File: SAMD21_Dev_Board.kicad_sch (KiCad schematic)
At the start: 76 parts, among them J1 SWD, J10 JST_SH_SM06B-SRSS-TB_1x06-1MP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, J11 JST_SH_SM06B-SRSS-TB_1x06-1MP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, J12 JST_SH_SM06B-SRSS-TB_1x06-1MP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, J13 JST_SH_SM06B-SRSS-TB_1x06-1MP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, J14 JST_SH_SM06B-SRSS-TB_1x06-1MP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, J15 JST_SH_SM06B-SRSS-TB_1x06-1MP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, J16 JST_SH_SM06B-SRSS-TB_1x06-1MP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, J17 Status LED, J2 USB_C_Receptacle_USB2.0_16P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

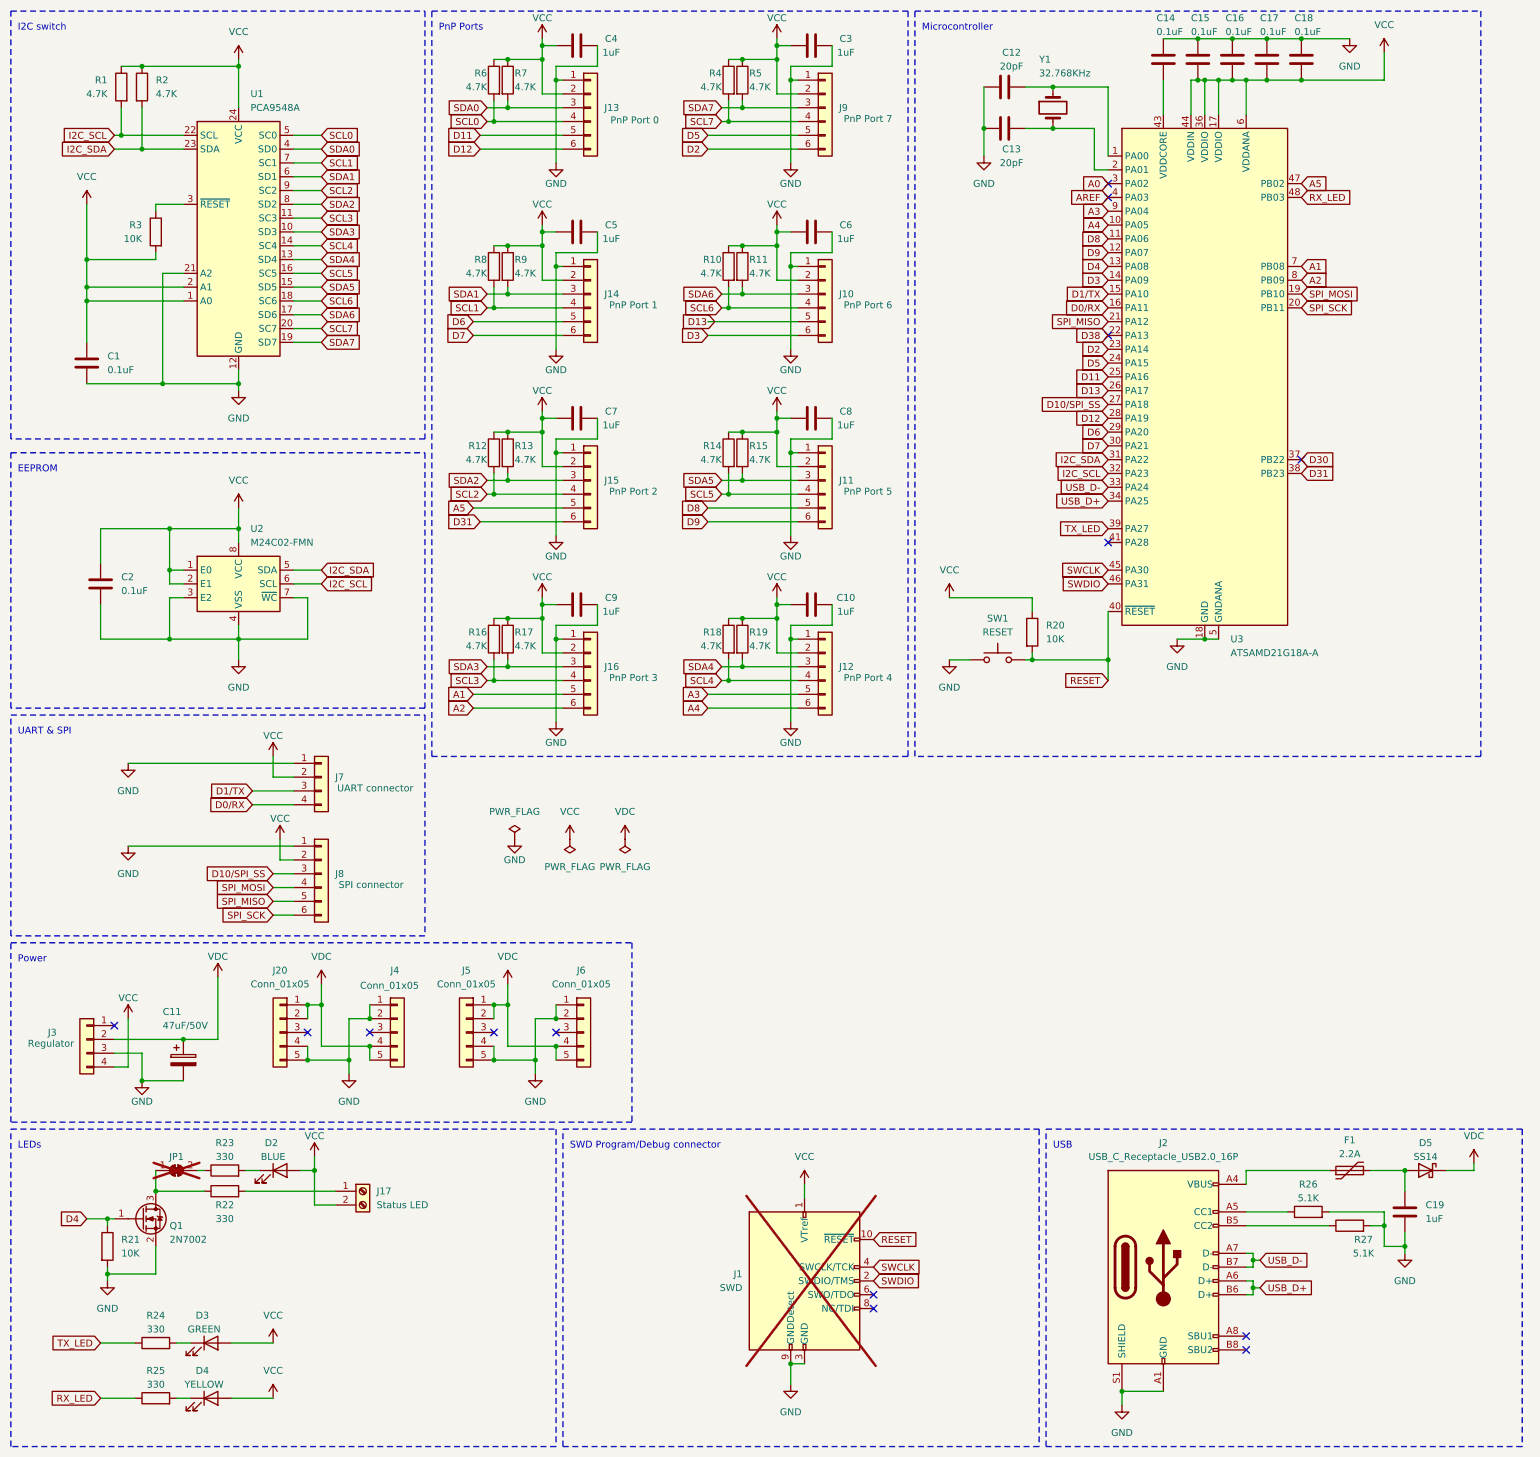
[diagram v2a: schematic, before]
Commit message: Power modules are set wider, to have more space for XT30 connectors. Interrupt lines were changed based on the SAMD21 interrupt mapping. PnP connector lines were swapped to match colors on the JST-SH-06 cables available from Pololu. Status LED line changed to be one of the lines that are left, that have PWM capability.
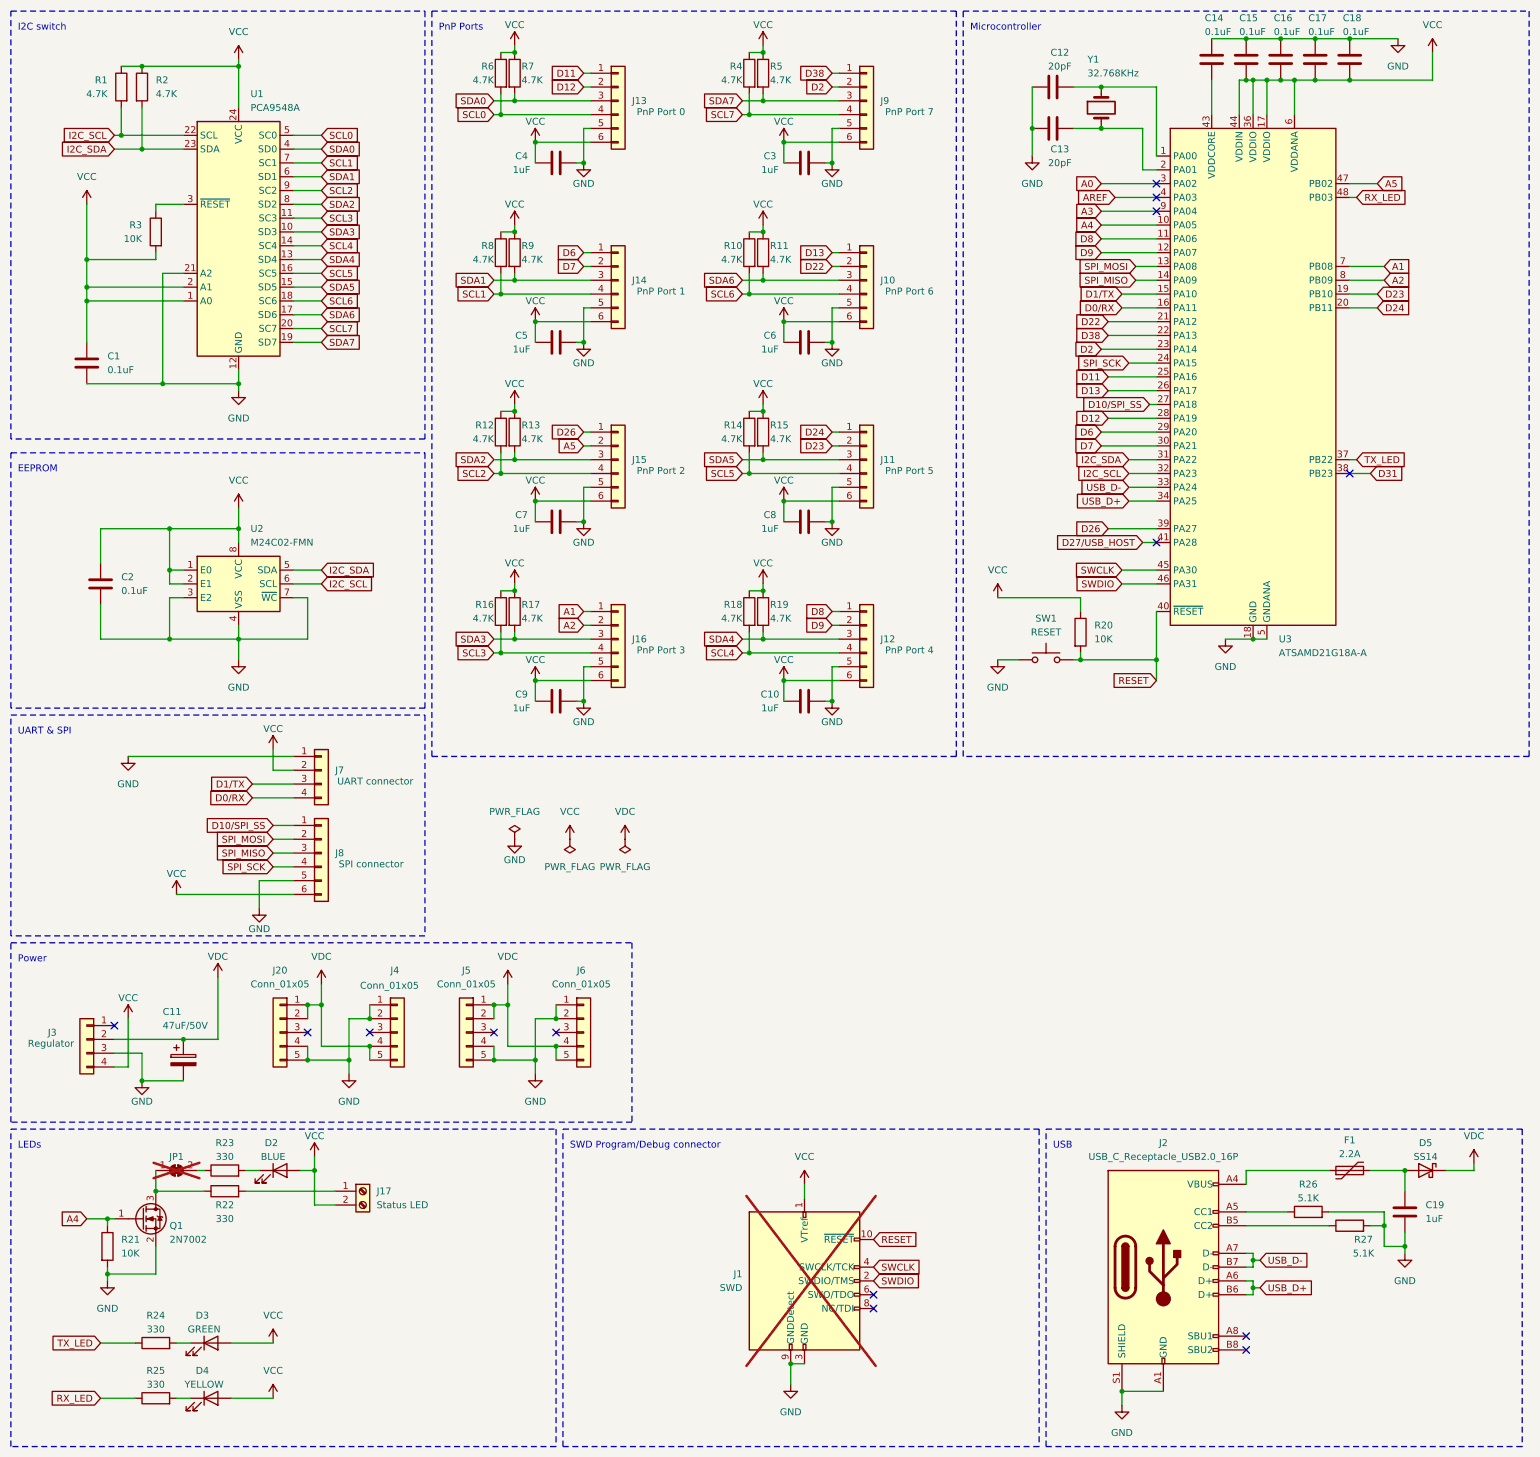
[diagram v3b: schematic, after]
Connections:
- net D30 is gone; now on net TX_LED: U3.37 (PB22)
- net A1: now also J16.1 (Pin_1); no longer J16.5 (Pin_5)
- net A2: now also J16.2 (Pin_2); no longer J16.6 (Pin_6)
- net A3: no longer J12.5 (Pin_5)
- net A4: now also Q1.1 (G), R21.1; no longer J12.6 (Pin_6)
- net A5: now also J15.2 (Pin_2); no longer J15.5 (Pin_5)
- net D10/SPI_SS: now also J8.1 (Pin_1); no longer J8.3 (Pin_3)
- net D11: now also J13.1 (Pin_1); no longer J13.5 (Pin_5)
- net D12: now also J13.2 (Pin_2); no longer J13.6 (Pin_6)
- net D13: now also J10.1 (Pin_1); no longer J10.5 (Pin_5)
- net D2: now also J9.2 (Pin_2); no longer J9.6 (Pin_6)
- net D31: no longer J15.6 (Pin_6)
- net D38: now also J9.1 (Pin_1)
- net D6: now also J14.1 (Pin_1); no longer J14.5 (Pin_5)
- net D7: now also J14.2 (Pin_2); no longer J14.6 (Pin_6)
- net D8: now also J12.1 (Pin_1); no longer J11.5 (Pin_5)
- net D9: now also J12.2 (Pin_2); no longer J11.6 (Pin_6)
- net GND: now also J10.5 (Pin_5), J11.5 (Pin_5), J12.5 (Pin_5), J13.5 (Pin_5), J14.5 (Pin_5), J15.5 (Pin_5), J16.5 (Pin_5), J8.5 (Pin_5), J9.5 (Pin_5); no longer J10.1 (Pin_1), J11.1 (Pin_1), J12.1 (Pin_1), J13.1 (Pin_1), J14.1 (Pin_1), J15.1 (Pin_1), J16.1 (Pin_1), J8.1 (Pin_1), J9.1 (Pin_1)
- net SPI_MISO: now also J8.3 (Pin_3), U3.14 (PA09); no longer J8.5 (Pin_5), U3.21 (PA12)
- net SPI_MOSI: now also J8.2 (Pin_2), U3.13 (PA08); no longer J8.4 (Pin_4), U3.19 (PB10)
- net SPI_SCK: now also J8.4 (Pin_4), U3.24 (PA15); no longer J8.6 (Pin_6), U3.20 (PB11)
- net TX_LED: no longer U3.39 (PA27)
- net VCC: now also J10.6 (Pin_6), J11.6 (Pin_6), J12.6 (Pin_6), J13.6 (Pin_6), J14.6 (Pin_6), J15.6 (Pin_6), J16.6 (Pin_6), J8.6 (Pin_6), J9.6 (Pin_6); no longer J10.2 (Pin_2), J11.2 (Pin_2), J12.2 (Pin_2), J13.2 (Pin_2), J14.2 (Pin_2), J15.2 (Pin_2), J16.2 (Pin_2), J8.2 (Pin_2), J9.2 (Pin_2)
- net D27/USB_HOST: now reaches U3.41 (PA28)
- removed net D3: J10.6 (Pin_6), U3.14 (PA09)
- removed net D4: Q1.1 (G), R21.1, U3.13 (PA08)
- removed net D5: J9.5 (Pin_5), U3.24 (PA15)
- new net D22: J10.2 (Pin_2), U3.21 (PA12)
- new net D23: J11.2 (Pin_2), U3.19 (PB10)
- new net D24: J11.1 (Pin_1), U3.20 (PB11)
- new net D26: J15.1 (Pin_1), U3.39 (PA27)
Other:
- moved on the sheet: C12, C13, C14, C15, C16, C17, C18, J7, J8, R20, SW1, U3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

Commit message: Kikit panelization
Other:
- title: PlugAndPlay SAMD21 Development Board -> PlugAndPlay SAMD21 Dev Board

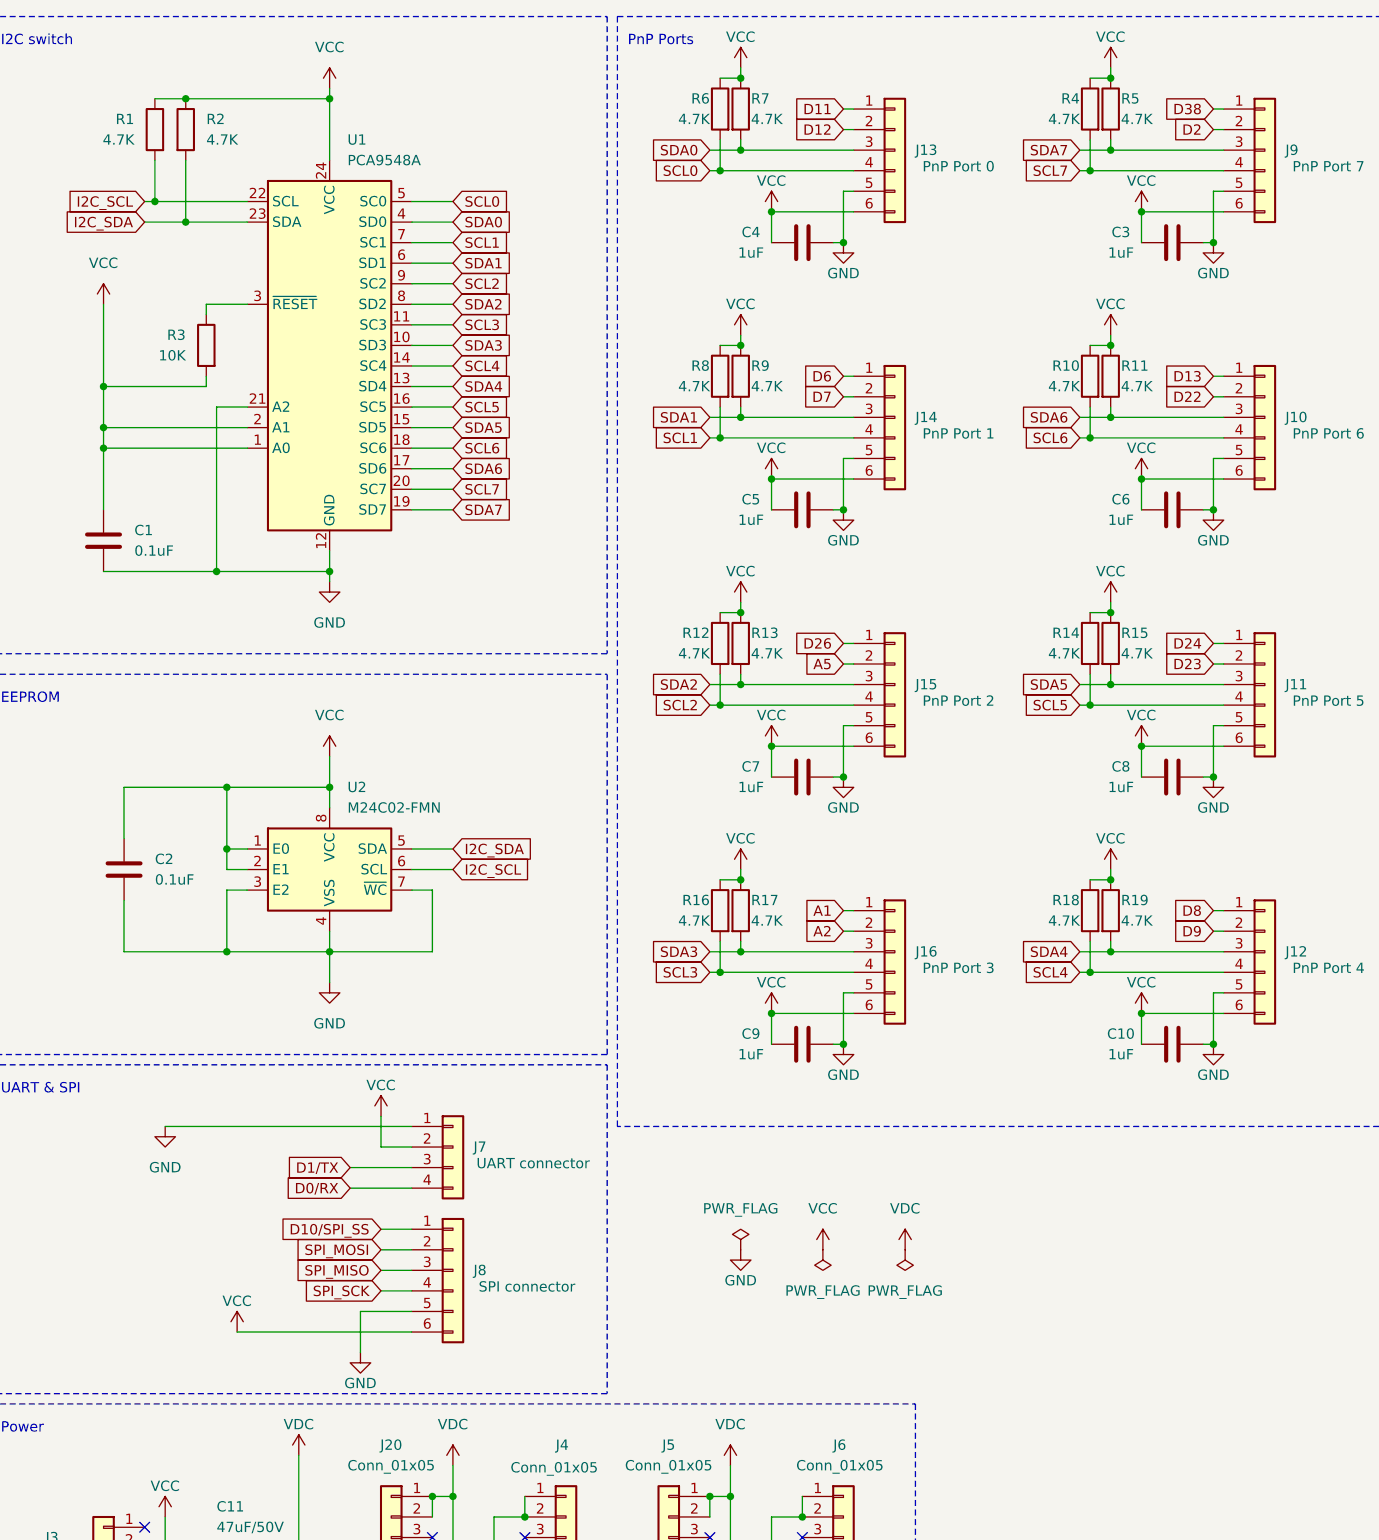
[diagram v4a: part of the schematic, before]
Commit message: Back to cables with GND pin1, VCC pin2
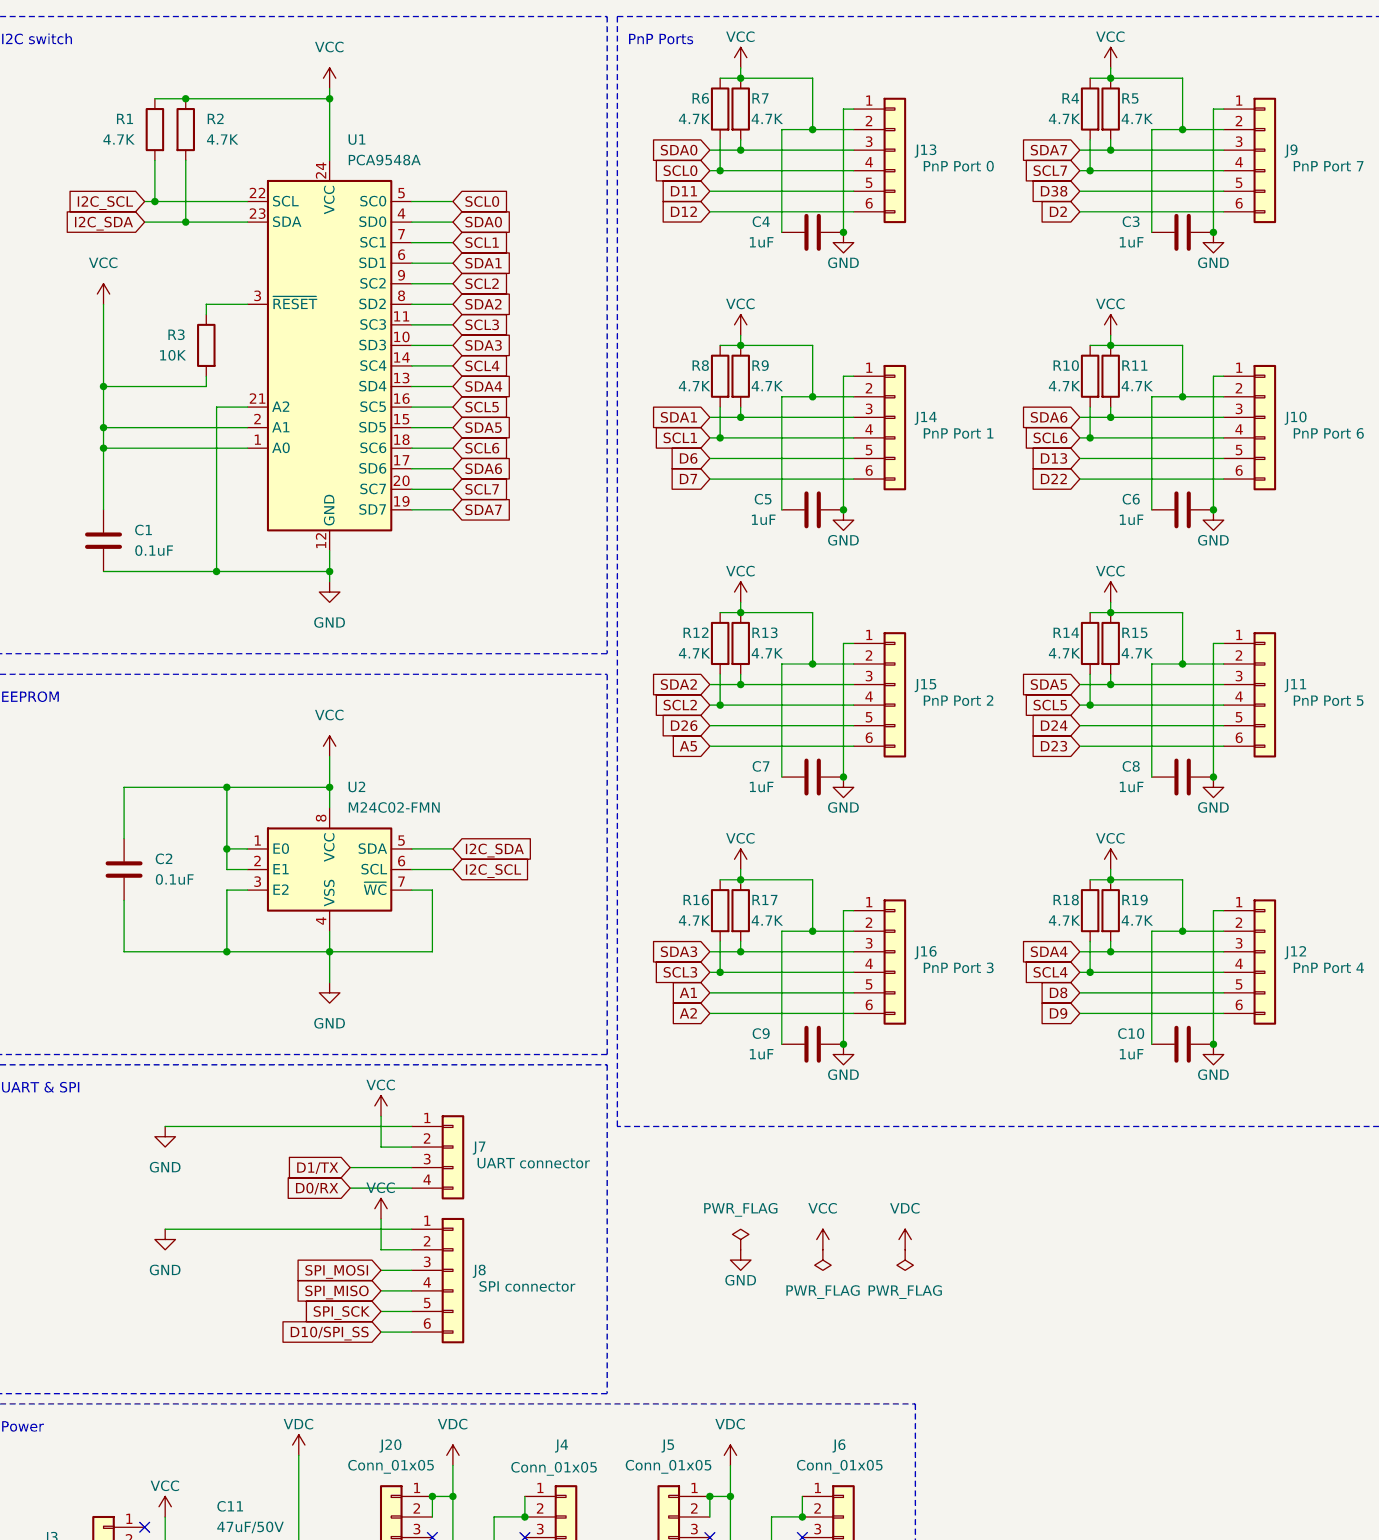
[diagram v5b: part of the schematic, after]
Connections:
- net A1: now also J16.5 (Pin_5); no longer J16.1 (Pin_1)
- net A2: now also J16.6 (Pin_6); no longer J16.2 (Pin_2)
- net A5: now also J15.6 (Pin_6); no longer J15.2 (Pin_2)
- net D10/SPI_SS: now also J8.6 (Pin_6); no longer J8.1 (Pin_1)
- net D11: now also J13.5 (Pin_5); no longer J13.1 (Pin_1)
- net D12: now also J13.6 (Pin_6); no longer J13.2 (Pin_2)
- net D13: now also J10.5 (Pin_5); no longer J10.1 (Pin_1)
- net D2: now also J9.6 (Pin_6); no longer J9.2 (Pin_2)
- net D22: now also J10.6 (Pin_6); no longer J10.2 (Pin_2)
- net D23: now also J11.6 (Pin_6); no longer J11.2 (Pin_2)
- net D24: now also J11.5 (Pin_5); no longer J11.1 (Pin_1)
- net D26: now also J15.5 (Pin_5); no longer J15.1 (Pin_1)
- net D38: now also J9.5 (Pin_5); no longer J9.1 (Pin_1)
- net D6: now also J14.5 (Pin_5); no longer J14.1 (Pin_1)
- net D7: now also J14.6 (Pin_6); no longer J14.2 (Pin_2)
- net D8: now also J12.5 (Pin_5); no longer J12.1 (Pin_1)
- net D9: now also J12.6 (Pin_6); no longer J12.2 (Pin_2)
- net GND: now also C5.2, J10.1 (Pin_1), J11.1 (Pin_1), J12.1 (Pin_1), J13.1 (Pin_1), J14.1 (Pin_1), J15.1 (Pin_1), J16.1 (Pin_1), J8.1 (Pin_1), J9.1 (Pin_1); no longer C5.1, J10.5 (Pin_5), J11.5 (Pin_5), J12.5 (Pin_5), J13.5 (Pin_5), J14.5 (Pin_5), J15.5 (Pin_5), J16.5 (Pin_5), J8.5 (Pin_5), J9.5 (Pin_5)
- net SPI_MISO: now also J8.4 (Pin_4); no longer J8.3 (Pin_3)
- net SPI_MOSI: now also J8.3 (Pin_3); no longer J8.2 (Pin_2)
- net SPI_SCK: now also J8.5 (Pin_5); no longer J8.4 (Pin_4)
- net VCC: now also C5.1, J10.2 (Pin_2), J11.2 (Pin_2), J12.2 (Pin_2), J13.2 (Pin_2), J14.2 (Pin_2), J15.2 (Pin_2), J16.2 (Pin_2), J8.2 (Pin_2), J9.2 (Pin_2); no longer C5.2, J10.6 (Pin_6), J11.6 (Pin_6), J12.6 (Pin_6), J13.6 (Pin_6), J14.6 (Pin_6), J15.6 (Pin_6), J16.6 (Pin_6), J8.6 (Pin_6), J9.6 (Pin_6)
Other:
- moved on the sheet: C10, C3, C4, C5, C6, C7, C8, C9
